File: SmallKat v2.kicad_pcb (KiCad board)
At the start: 4 copper layers, 104 x 56 mm, 272 parts, among them IC1 TPS562201DDCR, IC2 TPS40192DRCT, IC4 MAX34409ETE+, IC5 MAX34409ETE+, IC6 MAX34409ETE+, IC7 MAX34409ETE+, J1 Conn_01x03_Male, J10 Conn_01x03_Male, J11 Conn_01x03_Male, J12 Conn_01x03_Male, J13 Conn_01x03_Male, J14 Conn_01x03_Male, J15 Conn_01x03_Male, J16 Conn_01x03_Male, J17 Conn_01x03_Male, J19 USB_C_Receptacle, J2 Conn_01x03_Male, J21 Conn_01x05_Male, J3 Conn_01x03_Male, J4 Conn_01x03_Male, J5 Conn_01x03_Male, J6 Conn_01x03_Male, J7 Conn_01x03_Male, J8 Conn_01x03_Male, J9 Conn_01x02_Male, Q1 BUK9M120-100EX, Q10 CSD17307Q5A, Q11 CSD17307Q5A, Q12 Si7141DP, Q2 BUK9M120-100EX, Q3 MMBT3904, Q4 MMBT3904, Q7 2N3905, Q8 BUK9M120-100EX, Q9 BUK9M120-100EX, SW1 SW_SPST, SW2 SW_SPST, SW5 SW_SPST, U1 BNO055, U11 FUSB302BMPX, U12 BQ24770, U13 bq76925, U14 PCA9641, U2 LM2840Y, U3 ESP32-WROOM-32, U4 CP2102N-A01-GQFN24, U6 STM32L432KBUx, Y1 32.768kHz

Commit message: order
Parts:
- removed C22: 1uF, Capacitor_SMD:C_0402_1005Metric
- removed D17: MA2YD26, Diode_SMD:D_SOD-123F
- removed IC2: TPS40192DRCT, TPS40192DRCT:SON50P300X300X100-11N
- removed TP8: TestPoint, TestPoint:TestPoint_Pad_D1.5mm
- added C30: 22uF, Capacitor_SMD:C_0805_2012Metric, F.Cu at (186.5, 112.3)
- added C33: 0.1uF, Capacitor_SMD:C_0402_1005Metric, F.Cu at (190.5, 105.4)
- added C34: 22uF, Capacitor_SMD:C_0805_2012Metric, F.Cu at (186.5, 110.4)
- added D6: LED, LED_SMD:LED_0603_1608Metric, F.Cu at (142.7, 139.4)
- added IC3: TPS562201DDCR, Package_TO_SOT_SMD:SOT-23-6, F.Cu at (187.7, 104.0)
- added R28: 10K, Resistor_SMD:R_0402_1005Metric, F.Cu at (187.7, 101.1)
- added R29: 2.74K, Resistor_SMD:R_0402_1005Metric, F.Cu at (144.6, 104.0)
- added R30: 29.4R, Resistor_SMD:R_0402_1005Metric, F.Cu at (128.4, 96.9)
- added R31: 330R, Resistor_SMD:R_0402_1005Metric, F.Cu at (143.1, 138.1)
- added TP4: TestPoint, TestPoint:TestPoint_Pad_D1.5mm, B.Cu at (156.7, 88.4)
- C10: value 1000pF -> 10uF; footprint Capacitor_SMD:C_0402_1005Metric -> Capacitor_SMD:C_1206_3216Metric
- C11: value 100pF -> 10uF; footprint Capacitor_SMD:C_0402_1005Metric -> Capacitor_SMD:C_1206_3216Metric
- C12: value 10nF -> 2.2uF
- C13: value 1uF -> 0.1uF
- C14: value 4.7uF -> 6.8nF
- C15: value 470nF -> 0.1uF
- C16: value 10uF -> 5.6nF; footprint Capacitor_SMD:C_1206_3216Metric -> Capacitor_SMD:C_0402_1005Metric
- C18: value 10uF -> 1pF; footprint Capacitor_SMD:C_1206_3216Metric -> Capacitor_SMD:C_0402_1005Metric
- C19: value 100uF -> 330pF; footprint Capacitor_SMD:C_1210_3225Metric -> Capacitor_SMD:C_0402_1005Metric
- C21: value 100uF -> 10uF; footprint Capacitor_SMD:C_1210_3225Metric -> Capacitor_SMD:C_0805_2012Metric
- C23: value 2.2uF -> 10uF
- C25: value 0.1uF -> 10uF; footprint Capacitor_SMD:C_0402_1005Metric -> Capacitor_SMD:C_0805_2012Metric
- C35: value 10uF -> 0.1uF; footprint Capacitor_SMD:C_0805_2012Metric -> Capacitor_SMD:C_0402_1005Metric
- IC1: footprint TPS562201DDCR:SOT95P280X110-6N -> Package_TO_SOT_SMD:SOT-23-6
- J21: moved to B.Cu
- L3: value 15uH -> 4.7uH; footprint Inductor_SMD:L_1210_3225Metric -> Inductor_SMD:L_0805_2012Metric
- L4: value L -> 2.2uH
- R12: value 2.18k -> 20K
- R13: value 20k -> 2.1R
- R14: value 2.61k -> 10K
- R15: value 4.22k -> 10K
- R16: value 3.9k -> 20K
- R17: value 100k -> 20K
- R18: value 100k -> 634R
- R19: value 100k -> 2.49K
- R2: value 1K -> 10K
- R20: value 20K -> 18K
- R3: value 3.4K -> 33.2K
- U2: value LM2840Y -> LM25145RGYR; footprint Package_TO_SOT_SMD:TSOT-23-6 -> LM25145:LM25145RGYR
- moved U2 39.0 mm to (149.3, 103.3), turned to 0 degrees
- moved C10 22.6 mm to (160.2, 95.0)
- moved C18 19.4 mm to (142.7, 103.0), turned to 270 degrees
- moved TP7 19.3 mm to (130.8, 102.4)
- moved R20 16.9 mm to (143.7, 104.0), turned to 90 degrees
- moved C11 16.8 mm to (160.2, 97.3), turned to 0 degrees
- moved C16 15.2 mm to (146.0, 102.6)
- moved R12 14.7 mm to (127.2, 98.2)
- moved R13 13.8 mm to (152.2, 100.0), turned to 180 degrees
- moved TP6 11.5 mm to (145.2, 88.3)
- moved C19 8.85 mm to (128.3, 98.9), turned to 270 degrees
- moved C12 8.75 mm to (152.7, 104.1), turned to 0 degrees
- moved R14 8.18 mm to (148.1, 100.0), turned to 180 degrees
- moved R19 7.81 mm to (144.1, 102.6), turned to 0 degrees
- moved C13 7.71 mm to (150.3, 100.0), turned to 180 degrees
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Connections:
- C10 pad 1: +6V -> +BATT
- C10 pad 2: Net-(C10-Pad2) -> GND
- C11 pad 1: Net-(C11-Pad1) -> +BATT
- C11 pad 2: Net-(C11-Pad2) -> GND
- C12 pad 1: Net-(C11-Pad1) -> Net-(C12-Pad1)
- C12 pad 2: Net-(C12-Pad2) -> GND
- C13 pad 1: +BATT -> Net-(C13-Pad1)
- C16 pad 1: +BATT -> Net-(C16-Pad1)
- C16 pad 2: GND -> Net-(C16-Pad2)
- C18 pad 1: +BATT -> Net-(C18-Pad1)
- C18 pad 2: GND -> Net-(C16-Pad2)
- C19 pad 1: +6V -> Net-(C19-Pad1)
- C23 pad 1: VBUS -> GND
- C23 pad 2: GND -> +BATT
- C25 pad 1: Net-(C25-Pad1) -> GND
- C25 pad 2: Net-(C25-Pad2) -> +BATT
- C35 pad 1: +3.3VA -> Net-(C35-Pad1)
- C35 pad 2: GND -> Net-(C35-Pad2)
- L3 pad 1: Net-(C25-Pad1) -> +3.3VA
- L3 pad 2: +3.3VA -> Net-(C35-Pad2)
- Q1 pad 4: Net-(IC2-Pad10) -> Net-(Q1-Pad4)
- Q2 pad 4: Net-(IC2-Pad7) -> Net-(Q2-Pad4)
- R12 pad 1: Net-(C11-Pad2) -> +6V
- R12 pad 2: GND -> Net-(D4-Pad2)
- R13 pad 1: +6V -> +BATT
- R13 pad 2: Net-(C11-Pad2) -> Net-(C13-Pad1)
- R14 pad 1: Net-(C11-Pad2) -> Net-(R14-Pad1)
- R14 pad 2: Net-(C10-Pad2) -> /MainBoard/6VEN
- R15 pad 1: Net-(C12-Pad2) -> Net-(R15-Pad1)
- R15 pad 2: Net-(C11-Pad2) -> GND
- R16 pad 1: Net-(C11-Pad1) -> Net-(R16-Pad1)
- R16 pad 2: GND -> Net-(C12-Pad1)
- R17 pad 1: /MainBoard/6VEN -> Net-(R17-Pad1)
- R17 pad 2: Net-(IC2-Pad1) -> Net-(C12-Pad1)
- R18 pad 1: Net-(C14-Pad1) -> Net-(C15-Pad1)
- R18 pad 2: Net-(IC2-Pad5) -> Net-(R18-Pad2)
- R19 pad 1: Net-(C15-Pad1) -> Net-(C18-Pad1)
- R19 pad 2: Net-(C15-Pad2) -> Net-(C16-Pad1)
- R2 pad 1: Net-(R2-Pad1) -> GND
- R2 pad 2: GND -> Net-(IC3-Pad4)
- R20 pad 2: Net-(D4-Pad2) -> Net-(C18-Pad1)
- R3 pad 2: Net-(R2-Pad1) -> Net-(IC3-Pad4)
- TP6 pad 1: +BATT -> GND
- TP7 pad 1: GND -> +6V
- U2 pad 1: Net-(C25-Pad2) -> Net-(R14-Pad1)
- U2 pad 2: GND -> Net-(R15-Pad1)
- U2 pad 3: Net-(R2-Pad1) -> Net-(C14-Pad1)
- U2 pad 4: VBUS -> Net-(C16-Pad2)
- U2 pad 5: VBUS -> Net-(C18-Pad1)
- U2 pad 6: Net-(C25-Pad1) -> GND
- U3 pad 39: (no net) -> GND
- U6 pad 18: (no net) -> Net-(R31-Pad2)
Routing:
- net +BATT: track 51.0 -> 79.8 mm, vias 10 -> 19
- net GND: track 116.1 -> 131.7 mm, vias 576 -> 532
- net VBUS: track 11.4 -> 0.00 mm, vias 416 -> 214
- net Net-(Q2-Pad4): track 0.00 -> 10.5 mm, vias 0 -> 2
- net Net-(C12-Pad1): track 0.00 -> 9.96 mm, vias 0 -> 2
- net Net-(R31-Pad2): track 0.00 -> 9.50 mm, vias 0 -> 2
- net Net-(C11-Pad2): track 7.95 -> 0.00 mm
- net Net-(IC2-Pad7): track 6.45 -> 0.00 mm, vias 3 -> 0
- net Net-(C16-Pad2): track 0.00 -> 6.34 mm, vias 0 -> 2
- net Net-(C18-Pad1): track 0.00 -> 6.24 mm
- net Net-(C25-Pad1): track 6.10 -> 0.00 mm
- net Net-(C11-Pad1): track 5.63 -> 0.00 mm, vias 2 -> 0
- net Net-(Q1-Pad4): track 0.00 -> 5.46 mm, vias 0 -> 2
- net Net-(C35-Pad2): track 0.00 -> 5.41 mm, vias 0 -> 2
- net Net-(IC2-Pad10): track 4.78 -> 0.00 mm, vias 1 -> 0
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
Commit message: Rev
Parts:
- removed C45, C46, C54, C55: 0.1uF, Capacitor_SMD:C_0402_1005Metric
- removed C82: 1uF, Capacitor_SMD:C_0402_1005Metric
- removed IC4, IC5, IC6, IC7: MAX34409ETE+, MAX34409ETE+:QFN65P400X400X80-17N
- removed Q4: MMBT3904, Package_TO_SOT_SMD:SOT-23
- removed R101, R102, R103, R106, R107, R108, R109, R111, R112, R113, R114, R59, R60, R64, R65, R67, R68, R71, R72, R76, R77, R81, R82, R84, R85, R89, R90, R93, R94, R95, R96, R98: 100R, Resistor_SMD:R_0402_1005Metric
- removed R110, R83, R97: 0R, Resistor_SMD:R_0402_1005Metric
- removed R126, R127, R43: 10K, Resistor_SMD:R_0402_1005Metric
- removed U14: PCA9641, Package_DFN_QFN:UQFN-16-1EP_4x4mm_P0.65mm_EP2.6x2.6mm
- removed U2: LM25145RGYR, LM25145:LM25145RGYR
- removed U6: STM32L432KBUx, Package_DFN_QFN:QFN-32-1EP_5x5mm_P0.5mm_EP3.45x3.45mm
- added C22: C, Capacitor_SMD:C_0402_1005Metric, F.Cu at (129.2, 114.6)
- added C36: C, Capacitor_SMD:C_0402_1005Metric, F.Cu at (129.3, 116.5)
- added C38: C, Capacitor_SMD:C_0402_1005Metric, F.Cu at (125.0, 119.9)
- added C39: 47uF, Capacitor_SMD:C_1206_3216Metric, F.Cu at (127.2, 92.6)
- added C40: 47uF, Capacitor_SMD:C_1206_3216Metric, F.Cu at (127.2, 90.4)
- added C41: 1uF, Capacitor_SMD:C_0402_1005Metric, F.Cu at (91.5, 85.2)
- added C42: 0.1uF, Capacitor_SMD:C_0402_1005Metric, F.Cu at (148.0, 123.5)
- added C43: 0.1uF, Capacitor_SMD:C_0402_1005Metric, F.Cu at (157.6, 94.8)
- added D9: LED, LED_SMD:LED_0603_1608Metric, F.Cu at (146.8, 108.7)
- added F5: Fuse, 01550900M:0154.250DR, F.Cu at (151.1, 113.2)
- added IC8: TPS40192DRCT-TPS40192DRCT, Package_SON:VSON-10-1EP_3x3mm_P0.5mm_EP1.2x2mm, F.Cu at (120.2, 95.5)
- added J18: Conn_01x03_Male, Connector_PinHeader_2.54mm:PinHeader_1x03_P2.54mm_Vertical, F.Cu at (160.0, 110.7)
- added J20: Conn_01x03_Male, Connector_PinHeader_2.54mm:PinHeader_1x03_P2.54mm_Vertical, F.Cu at (160.0, 105.7)
- added J22: Conn_01x03_Male, Connector_PinHeader_2.54mm:PinHeader_1x03_P2.54mm_Vertical, F.Cu at (160.0, 108.2)
- added J23: Conn_01x03_Male, Connector_PinHeader_2.54mm:PinHeader_1x03_P2.54mm_Vertical, F.Cu at (160.0, 103.1)
- added PS1: PAC1934T-I_JQ, PAC1934T-I_JQ:QFN65P400X400X55-17N-D, F.Cu at (83.7, 93.5)
- added PS2: PAC1934T-I_JQ, PAC1934T-I_JQ:QFN65P400X400X55-17N-D, F.Cu at (84.9, 113.6)
- added PS3: PAC1934T-I_JQ, PAC1934T-I_JQ:QFN65P400X400X55-17N-D, F.Cu at (84.1, 127.3)
- added PS4: PAC1934T-I_JQ, PAC1934T-I_JQ:QFN65P400X400X55-17N-D, F.Cu at (149.0, 126.7)
- added PS5: PAC1934T-I_JQ, PAC1934T-I_JQ:QFN65P400X400X55-17N-D, F.Cu at (158.3, 98.0)
- added R128: 20K, Resistor_SMD:R_0402_1005Metric, F.Cu at (147.6, 110.4)
- added R32: 3.3K, Resistor_SMD:R_0402_1005Metric, F.Cu at (126.9, 119.9)
- added R33: 0.01R, Resistor_SMD:R_0603_1608Metric, F.Cu at (156.7, 112.5)
- added R34: 0.01R, Resistor_SMD:R_0603_1608Metric, F.Cu at (156.7, 106.9)
- added R35: 0.01R, Resistor_SMD:R_0603_1608Metric, F.Cu at (156.7, 109.4)
- added R36: 0.01R, Resistor_SMD:R_0603_1608Metric, F.Cu at (156.7, 104.5)
- added R39: 0R, Resistor_SMD:R_0402_1005Metric, F.Cu at (148.2, 129.7)
- added R40: 0R, Resistor_SMD:R_0402_1005Metric, F.Cu at (157.2, 101.1)
- added TP8: TestPoint, TestPoint:TestPoint_Pad_D1.5mm, B.Cu at (120.8, 118.0)
- added U5: LPC824M201JHI33, Package_DFN_QFN:QFN-32-1EP_5x5mm_P0.5mm_EP3.45x3.45mm, F.Cu at (125.6, 115.6)
- added U7: TLC5947RHB, Package_DFN_QFN:QFN-32-1EP_5x5mm_P0.5mm_EP3.45x3.45mm, F.Cu at (125.3, 123.6)
- C10: value 10uF -> 1000pF; footprint Capacitor_SMD:C_1206_3216Metric -> Capacitor_SMD:C_0402_1005Metric
- C11: value 10uF -> 100pF; footprint Capacitor_SMD:C_1206_3216Metric -> Capacitor_SMD:C_0402_1005Metric
- C12: value 2.2uF -> 10nF
- C13: value 0.1uF -> 1uF
- C14: value 6.8nF -> 4.7uF
- C15: value 0.1uF -> 470nF
- C16: value 5.6nF -> 10uF; footprint Capacitor_SMD:C_0402_1005Metric -> Capacitor_SMD:C_1206_3216Metric
- C18: value 1pF -> 10uF; footprint Capacitor_SMD:C_0402_1005Metric -> Capacitor_SMD:C_1206_3216Metric
- C19: value 330pF -> 100uF; footprint Capacitor_SMD:C_0402_1005Metric -> Capacitor_SMD:C_1210_3225Metric
- C21: value 10uF -> 100uF; footprint Capacitor_SMD:C_0805_2012Metric -> Capacitor_SMD:C_1210_3225Metric
- C69, C74: footprint Capacitor_SMD:C_0402_1005Metric -> Capacitor_SMD:C_0805_2012Metric
- H1, H2, H3, H4: footprint MountingHole:MountingHole_2.7mm_M2.5_Pad_Via -> MountingHole:MountingHole_3.2mm_M3_Pad_Via
- J19: footprint Connector_USB:USB_C_Receptacle_Amphenol_12401610E4-2A_CircularHoles -> C167321:C167321
- J9: footprint SmallKat ESP32:SHDR2W320P716_1X2_1574X813X1588P -> XT30PB:XT30PB
- Q3: value MMBT3904 -> MBT3904DW1; footprint Package_TO_SOT_SMD:SOT-23 -> Package_TO_SOT_SMD:SOT-363_SC-70-6
- R12: value 20K -> 2.18k
- R123: footprint Resistor_SMD:R_0603_1608Metric -> Resistor_SMD:R_0805_2012Metric
- R13: value 2.1R -> 20k
- R14: value 10K -> 2.61k
- R15: value 10K -> 4.22k
- R16: value 20K -> 3.9k
- R17: value 20K -> 100k
- R18: value 634R -> 100k
- R19: value 2.49K -> 100k
- R20: value 18K -> 1K
- R29: value 2.74K -> 0R
- R30: value 29.4R -> 0R
- TP4, TP6, TP7: footprint TestPoint:TestPoint_Pad_D1.5mm -> TestPoint:TestPoint_Pad_D2.5mm
- moved J2 119.1 mm to (76.2, 119.9), turned to 270 degrees
- moved J8 118.8 mm to (76.2, 127.5), turned to 270 degrees
- moved J4 118.8 mm to (76.2, 122.4), turned to 270 degrees
- moved J6 118.7 mm to (76.2, 125.0), turned to 270 degrees
- moved R62 112.4 mm to (79.6, 121.1), turned to 0 degrees
- moved R80 112.0 mm to (79.5, 129.0), turned to 0 degrees
- moved R70 111.9 mm to (79.6, 123.7), turned to 0 degrees
- moved R75 111.8 mm to (79.5, 126.2), turned to 0 degrees
- moved H1 103.9 mm to (71.8, 85.4)
- moved F3 101.9 mm to (80.6, 134.4), turned to 180 degrees
- moved R78 100.5 mm to (87.7, 135.4), turned to 270 degrees
- moved D25 99.6 mm to (89.0, 135.1), turned to 270 degrees
- moved C52 88.1 mm to (85.0, 130.5)
- moved R2 73.8 mm to (116.7, 100.8), turned to 270 degrees
- moved R28 71.8 mm to (115.9, 102.9)
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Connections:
- C10 pad 1: +BATT -> +6V
- C10 pad 2: GND -> Net-(C10-Pad2)
- C11 pad 1: +BATT -> Net-(C11-Pad1)
- C11 pad 2: GND -> Net-(C11-Pad2)
- C12 pad 1: Net-(C12-Pad1) -> Net-(C11-Pad1)
- C12 pad 2: GND -> Net-(C12-Pad2)
- C13 pad 1: Net-(C13-Pad1) -> +BATT
- C16 pad 1: Net-(C16-Pad1) -> +BATT
- C16 pad 2: Net-(C16-Pad2) -> GND
- C18 pad 1: Net-(C18-Pad1) -> +BATT
- C18 pad 2: Net-(C16-Pad2) -> GND
- C19 pad 1: Net-(C19-Pad1) -> +6V
- C37 pad 1: +3.3VA -> +3V3
- Q3 pad 1: Net-(Q3-Pad1) -> /MainBoard/ESP32Module/RTS
- Q3 pad 2: /MainBoard/ESP32Module/RTS -> Net-(Q3-Pad2)
- Q3 pad 3: /MainBoard/ESP32Module/EN -> /MainBoard/ESP32Module/DTR
- R12 pad 1: +6V -> Net-(C11-Pad2)
- R12 pad 2: Net-(D4-Pad2) -> GND
- R13 pad 1: +BATT -> +6V
- R13 pad 2: Net-(C13-Pad1) -> Net-(C11-Pad2)
- R14 pad 1: Net-(R14-Pad1) -> Net-(C11-Pad2)
- R14 pad 2: /MainBoard/6VEN -> Net-(C10-Pad2)
- R15 pad 1: Net-(R15-Pad1) -> Net-(C12-Pad2)
- R15 pad 2: GND -> Net-(C11-Pad2)
- R16 pad 1: Net-(R16-Pad1) -> Net-(C11-Pad1)
- R16 pad 2: Net-(C12-Pad1) -> GND
- R17 pad 1: Net-(R17-Pad1) -> /MainBoard/6VEN
- R17 pad 2: Net-(C12-Pad1) -> Net-(IC8-Pad1)
- R18 pad 1: Net-(C15-Pad1) -> Net-(C14-Pad1)
- R19 pad 1: Net-(C18-Pad1) -> Net-(C15-Pad1)
- R19 pad 2: Net-(C16-Pad1) -> Net-(C15-Pad2)
- R20 pad 2: Net-(C18-Pad1) -> Net-(D4-Pad2)
- R21 pad 1: /MainBoard/SERVO0 -> /MainBoard/NRST
- R25 pad 1: Net-(Q3-Pad1) -> Net-(Q3-Pad2)
- R26 pad 1: Net-(Q4-Pad1) -> Net-(Q3-Pad5)
- R29 pad 1: Net-(C18-Pad1) -> Net-(PS2-Pad6)
- R29 pad 2: GND -> +3V3
- R30 pad 1: +6V -> Net-(PS3-Pad6)
- R30 pad 2: Net-(C19-Pad1) -> +3V3
- R66 pad 1: +3V3 -> Net-(PS1-Pad6)
- R66 pad 2: Net-(IC4-Pad14) -> +3V3
- TP4 pad 1: +BATT -> +6V
- TP6 pad 1: GND -> +BATT
- TP7 pad 1: +6V -> GND
- U3 pad 10: /MainBoard/SERVO4 -> (no net)
- U3 pad 11: /MainBoard/SERVO3 -> (no net)
- U3 pad 12: /MainBoard/SERVO2 -> /MainBoard/TX1
- U3 pad 13: /MainBoard/SERVO1 -> /MainBoard/RX1
- U3 pad 14: /MainBoard/SERVO0 -> /MainBoard/NRST
- U3 pad 16: /MainBoard/SERVO8 -> /MainBoard/TALKALLOWED
- U3 pad 23: /MainBoard/SERVO9 -> (no net)
- U3 pad 24: /MainBoard/SERVO10 -> (no net)
- U3 pad 26: /MainBoard/SERVO11 -> (no net)
- U3 pad 27: /MainBoard/SERVO12 -> (no net)
- U3 pad 28: /MainBoard/SERVO13 -> (no net)
- U3 pad 29: /MainBoard/SERVO14 -> (no net)
- U3 pad 30: /MainBoard/SERVO15 -> (no net)
- U3 pad 31: /MainBoard/SERVO7 -> (no net)
- U3 pad 8: /MainBoard/SERVO6 -> (no net)
- U3 pad 9: /MainBoard/SERVO5 -> (no net)
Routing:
- net /MainBoard/_SCL: track 131.4 -> 0.00 mm, vias 6 -> 0
- net /MainBoard/_SDA: track 128.6 -> 0.00 mm, vias 7 -> 0
- net /MainBoard/SCL: track 38.7 -> 154.9 mm, vias 5 -> 14
- net /MainBoard/SDA: track 39.6 -> 155.3 mm, vias 5 -> 13
- net /MainBoard/Servos/6V4: track 111.9 -> 3.60 mm, vias 104 -> 0
- net /MainBoard/Servos/6V1: track 104.9 -> 0.00 mm, vias 164 -> 0
- net /MainBoard/Servos/6V3: track 90.1 -> 4.12 mm, vias 71 -> 0
- net /MainBoard/SERVO0: track 16.4 -> 98.7 mm, vias 1 -> 2
- net /MainBoard/Servos/6V2: track 66.7 -> 3.92 mm, vias 64 -> 0
- net Net-(R24-Pad2): track 7.54 -> 62.5 mm, vias 2 -> 5
- net /MainBoard/SERVO1: track 17.8 -> 61.6 mm, vias 1 -> 2
- net /MainBoard/SERVO19: track 0.00 -> 43.4 mm, vias 0 -> 1
- net +3.3VA: track 63.7 -> 21.7 mm, vias 19 -> 4
- net /MainBoard/SERVO18: track 0.00 -> 41.2 mm, vias 0 -> 1
- net /MainBoard/SERVO2: track 20.9 -> 60.8 mm, vias 1 -> 2
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- added copper zone on F.Cu, net /MainBoard/Servos/6V1
- added copper zone on F.Cu, net /MainBoard/Servos/6V2
- added copper zone on F.Cu, net /MainBoard/Servos/6V3
- added copper zone on F.Cu, net /MainBoard/Servos/6V4
- added copper zone on F.Cu, net /MainBoard/Servos/6V5
- removed copper zone on In1.Cu, net +3.3VA
- removed copper zone on In1.Cu, net GND
- removed copper zone on F.Cu, net Net-(C50-Pad2)
- removed copper zone on F.Cu, net Net-(C57-Pad1)
- removed copper zone on In1.Cu, net VBUS
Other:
- board size 104 x 56 mm -> 100 x 56 mm
- net class Default: clearance 0.127 -> 0.1778; trace_width 0.127 -> 0.1778
- rule trace_clearance: 0.127 -> 0.1778
- board text removed: "+"
- board text removed: "BATT+"
- board text removed: "Elbow"
- board text removed: "Fuse Good"
- board text removed: "Head Pan"
- board text removed: "Head Tilt"
- board text removed: "Pan"
- board text removed: "Tail Pan"
- board text removed: "Tail Tilt"
- board text removed: "Tilt"

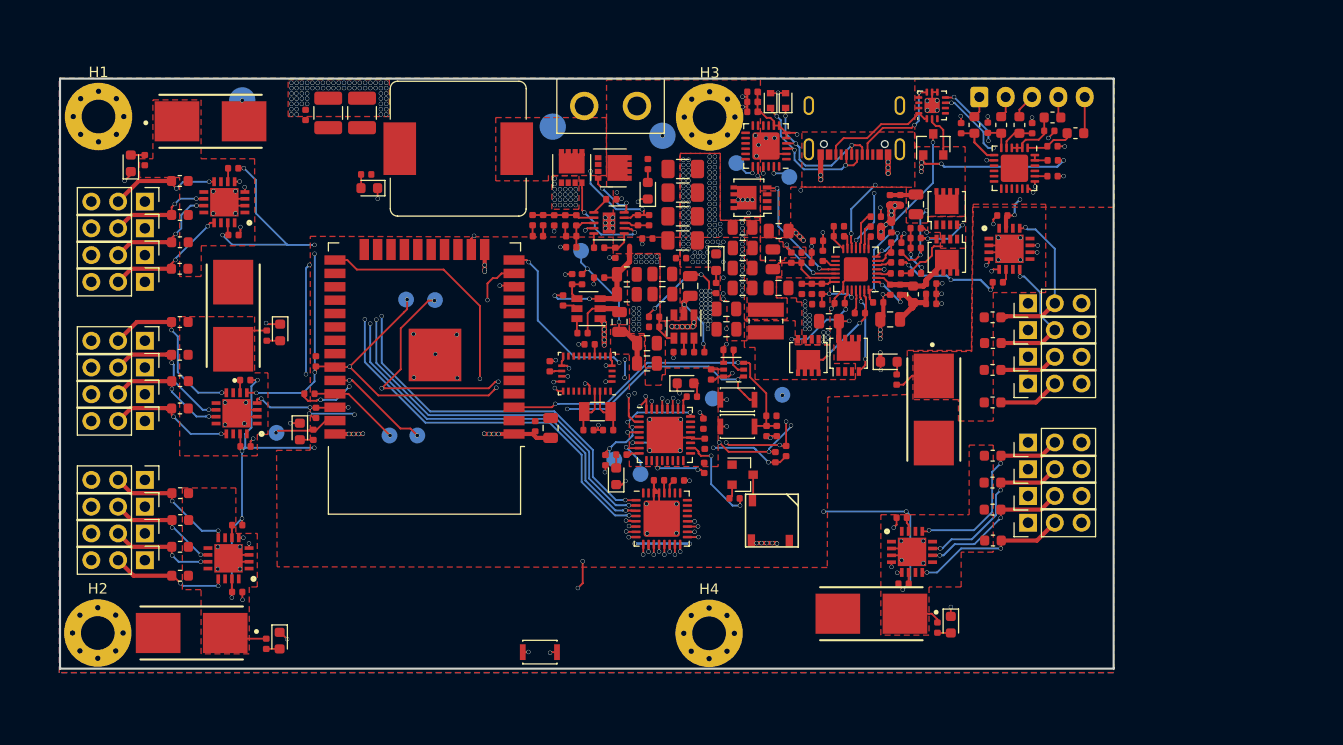
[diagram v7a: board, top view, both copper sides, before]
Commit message: This rev removes the safety micro and instead uses the dji battery
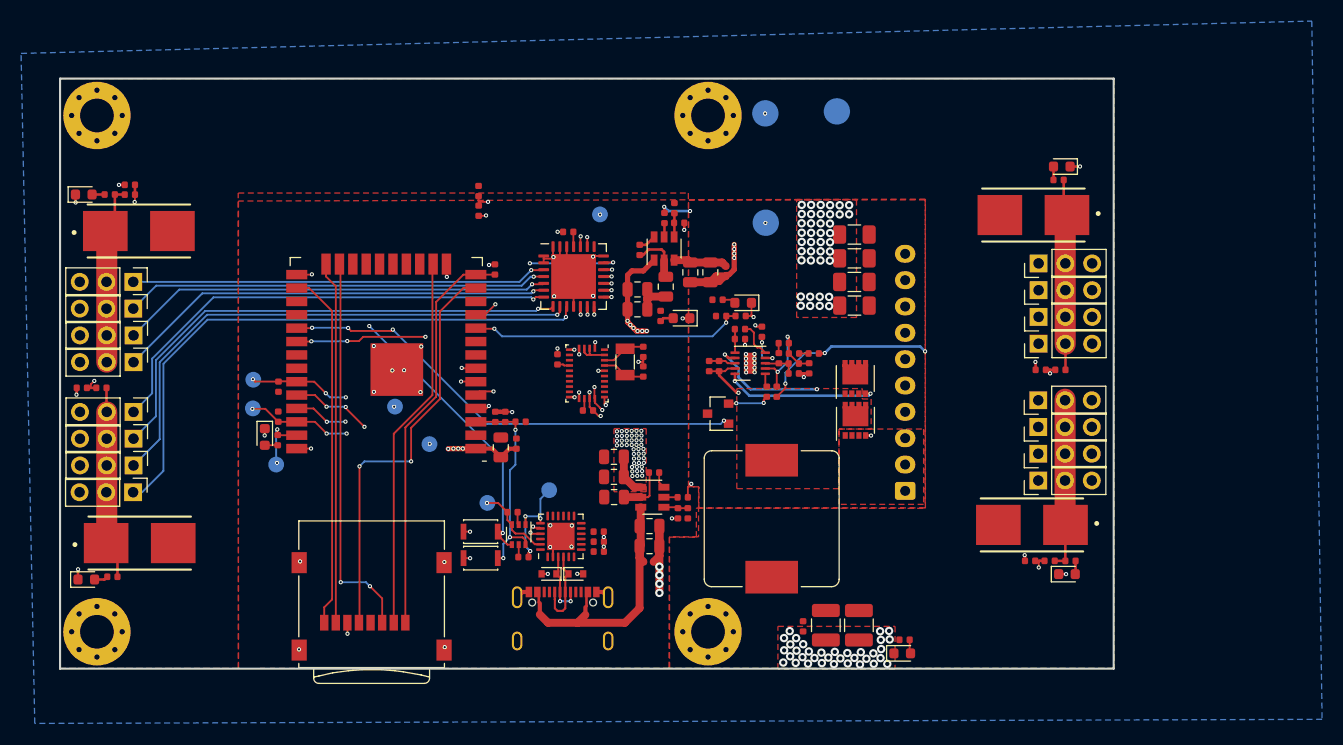
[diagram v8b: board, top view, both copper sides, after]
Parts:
- removed BZ1: Buzzer, KLJ-5030:KLJ-5030
- removed C34, C72, C75, C76, C77: 22uF, Capacitor_SMD:C_0805_2012Metric
- removed C35, C37, C42, C43, C49, C51, C52, C53, C57, C59, C64, C70, C71, C73, C78, C79, C80: 0.1uF, Capacitor_SMD:C_0402_1005Metric
- removed C36, C38: C, Capacitor_SMD:C_0402_1005Metric
- removed C47: 2.2uF, Capacitor_SMD:C_0805_2012Metric
- removed C48: 2200pF, Capacitor_SMD:C_0402_1005Metric
- removed C50, C60, C61, C65, C81: 1uF, Capacitor_SMD:C_0402_1005Metric
- removed C56, C58: 100pF, Capacitor_SMD:C_0402_1005Metric
- removed C62: 0.01uF, Capacitor_SMD:C_0402_1005Metric
- removed C63, C66, C69, C74: 10uF, Capacitor_SMD:C_0805_2012Metric
- removed C67: 470pF, Capacitor_SMD:C_0402_1005Metric
- removed C68: 0.047uF, Capacitor_SMD:C_0402_1005Metric
- removed D18, D6, D9: LED, LED_SMD:LED_0603_1608Metric
- removed D5: BAT54C, Package_TO_SOT_SMD:SOT-23
- removed F5: Fuse, 01550900M:0154.250DR
- removed IC3: TPS562201DDCR, Package_TO_SOT_SMD:SOT-23-6
- removed J20, J22, J23: Conn_01x03_Male, Connector_PinHeader_2.54mm:PinHeader_1x03_P2.54mm_Vertical
- removed J21: Conn_01x05_Male, Connector_JST:JST_EH_S5B-EH_1x05_P2.50mm_Horizontal
- removed L4: 2.2uH, Inductor_SMD:L_Wuerth_MAPI-3020
- removed PS1, PS2, PS3, PS4, PS5: PAC1934T-I_JQ, PAC1934T-I_JQ:QFN65P400X400X55-17N-D
- removed Q10, Q11: CSD17307Q5A, Package_TO_SOT_SMD:LFPAK33
- removed Q12: Si7141DP, Package_TO_SOT_SMD:LFPAK33
- removed Q7: 2N3905, Package_TO_SOT_SMD:SOT-23
- removed Q8, Q9: BUK9M120-100EX, Package_TO_SOT_SMD:LFPAK33
- removed R100, R104, R105, R57, R61, R62, R69, R70, R74, R75, R79, R80, R87, R88, R91, R92, R99: 0.01R, Resistor_SMD:R_0603_1608Metric
- removed R117, R119, R125, R45, R46, R47, R48, R56: 10K, Resistor_SMD:R_0402_1005Metric
- removed R118: 3M, Resistor_SMD:R_0402_1005Metric
- removed R120: 316K, Resistor_SMD:R_0402_1005Metric
- removed R121: 100K, Resistor_SMD:R_0402_1005Metric
- removed R122: 10R, Resistor_SMD:R_0402_1005Metric
- removed R123: 0.01R, Resistor_SMD:R_0805_2012Metric
- removed R124: 47R, Resistor_SMD:R_0603_1608Metric
- removed R128: 20K, Resistor_SMD:R_0402_1005Metric
- removed R24: 470R, Resistor_SMD:R_0402_1005Metric
- removed R39, R40, R66: 0R, Resistor_SMD:R_0402_1005Metric
- removed R44: 330R, Resistor_SMD:R_0402_1005Metric
- removed R49, R52: 3.9K, Resistor_SMD:R_0402_1005Metric
- removed R50: 430K, Resistor_SMD:R_0402_1005Metric
- removed R51: 66.5K, Resistor_SMD:R_0402_1005Metric
- removed R53: 4.7R, Resistor_SMD:R_0402_1005Metric
- removed R54, R55: 4.02K, Resistor_SMD:R_0402_1005Metric
- removed R58: 30.1K, Resistor_SMD:R_0402_1005Metric
- removed SW5: SW_SPST, Button_Switch_SMD:SW_SPST_CK_KXT3
- removed TP20, TP21, TP22, TP23, TP8: TestPoint, TestPoint:TestPoint_Pad_D1.5mm
- removed U11: FUSB302BMPX, Package_DFN_QFN:WQFN-14-1EP_2.5x2.5mm_P0.5mm_EP1.45x1.45mm
- removed U12: BQ24770, Package_DFN_QFN:QFN-28-1EP_4x4mm_P0.4mm_EP2.3x2.3mm
- removed U13: bq76925, Package_DFN_QFN:QFN-24-1EP_4x4mm_P0.5mm_EP2.6x2.6mm
- removed U5: LPC824M201JHI33, Package_DFN_QFN:QFN-32-1EP_5x5mm_P0.5mm_EP3.45x3.45mm
- removed U7: TLC5947RHB, Package_DFN_QFN:QFN-32-1EP_5x5mm_P0.5mm_EP3.45x3.45mm
- added IC2: TPS562201DDCR, Package_TO_SOT_SMD:SOT-23-6, F.Cu at (124.4, 121.5)
- added Q5: DMG2301L, Package_TO_SOT_SMD:SOT-23, F.Cu at (130.6, 113.6)
- added U2: PCA9685BS, Package_DFN_QFN:QFN-28-1EP_6x6mm_P0.65mm_EP4.25x4.25mm, F.Cu at (116.9, 100.6)
- C20: value 0.1uF -> 10uF; footprint Capacitor_SMD:C_0402_1005Metric -> Capacitor_SMD:C_0805_2012Metric
- C22: value C -> 10uF; footprint Capacitor_SMD:C_0402_1005Metric -> Capacitor_SMD:C_0805_2012Metric
- C23: value 10uF -> 22uF
- C25: value 10uF -> 0.1uF; footprint Capacitor_SMD:C_0805_2012Metric -> Capacitor_SMD:C_0402_1005Metric
- J18: value Conn_01x03_Male -> Micro_SD_Card; footprint Connector_PinHeader_2.54mm:PinHeader_1x03_P2.54mm_Vertical -> Connector_Card:microSD_HC_Wuerth_693072010801
- J9: value Conn_01x02_Male -> Conn_01x10_Female; footprint XT30PB:XT30PB -> Connector_JST:JST_EH_B10B-EH-A_1x10_P2.50mm_Vertical; moved to B.Cu
- R22, R37: value 47R -> 10K; footprint Resistor_SMD:R_0603_1608Metric -> Resistor_SMD:R_0402_1005Metric
- R23, R38: value 47R -> 8.2K; footprint Resistor_SMD:R_0603_1608Metric -> Resistor_SMD:R_0402_1005Metric
- R29: value 0R -> 33.2K
- R3: value 33.2K -> 2.4K
- R30: value 0R -> 10K
- R31: value 330R -> 10K
- R32: value 3.3K -> 8.2K
- R33, R35: value 0.01R -> 10K; footprint Resistor_SMD:R_0603_1608Metric -> Resistor_SMD:R_0402_1005Metric
- R34, R36: value 0.01R -> 8.2K; footprint Resistor_SMD:R_0603_1608Metric -> Resistor_SMD:R_0402_1005Metric
- moved R34 86.6 mm to (70.2, 111.2)
- moved J8 86.1 mm to (161.0, 112.3), turned to 90 degrees
- moved J6 85.4 mm to (161.0, 114.9), turned to 90 degrees
- moved J4 84.9 mm to (161.0, 117.4), turned to 90 degrees
- moved J2 84.8 mm to (161.0, 119.9), turned to 90 degrees
- moved R33 84.6 mm to (72.1, 111.2)
- moved F3 80.4 mm to (160.4, 124.2)
- moved R78 76.7 mm to (164.0, 127.6), turned to 0 degrees
- moved H4 76.1 mm to (71.7, 85.3)
- moved D25 75.0 mm to (163.7, 128.8), turned to 0 degrees
- moved C21 67.8 mm to (140.8, 133.7), turned to 270 degrees
- moved C19 67.7 mm to (144.0, 133.7), turned to 270 degrees
- moved C41 67.7 mm to (138.7, 133.8), turned to 270 degrees
- moved R20 67.5 mm to (148.3, 135.1), turned to 0 degrees
- moved D4 67.1 mm to (148.1, 136.3), turned to 0 degrees
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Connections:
- C17 pad 1: Net-(C17-Pad1) -> +3V3
- C20 pad 1: Net-(C20-Pad1) -> GND
- C20 pad 2: GND -> VBUS
- C22 pad 2: +3.3VA -> VBUS
- C23 pad 1: GND -> +3V3
- C23 pad 2: +BATT -> GND
- C25 pad 2: +BATT -> VBUS
- C30 pad 1: +3.3VA -> +3V3
- C33 pad 1: GND -> Net-(C33-Pad1)
- C33 pad 2: +BATT -> Net-(C33-Pad2)
- H3 pad 1: +BATT -> +6V
- J1 pad 2: /MainBoard/Servos/S1 -> /MainBoard/Servos/6V1
- J10 pad 2: /MainBoard/Servos/S5 -> /MainBoard/Servos/6V2
- J11 pad 2: /MainBoard/Servos/S13 -> /MainBoard/Servos/6V4
- J12 pad 2: /MainBoard/Servos/S6 -> /MainBoard/Servos/6V2
- J13 pad 2: /MainBoard/Servos/S14 -> /MainBoard/Servos/6V4
- J14 pad 2: /MainBoard/Servos/S7 -> /MainBoard/Servos/6V2
- J15 pad 2: /MainBoard/Servos/S15 -> /MainBoard/Servos/6V4
- J16 pad 2: /MainBoard/Servos/S8 -> /MainBoard/Servos/6V2
- J17 pad 2: /MainBoard/Servos/S16 -> /MainBoard/Servos/6V4
- J18 pad 1: /MainBoard/SERVO16 -> /MainBoard/IO12
- J18 pad 2: /MainBoard/Servos/S17 -> /MainBoard/IO13
- J18 pad 3: GND -> /MainBoard/IO15
- J19 pad A5: /MainBoard/CC1 -> (no net)
- J19 pad B5: /MainBoard/CC2 -> (no net)
- J2 pad 2: /MainBoard/Servos/S9 -> /MainBoard/Servos/6V3
- J3 pad 2: /MainBoard/Servos/S2 -> /MainBoard/Servos/6V1
- J4 pad 2: /MainBoard/Servos/S10 -> /MainBoard/Servos/6V3
- J5 pad 2: /MainBoard/Servos/S3 -> /MainBoard/Servos/6V1
- J6 pad 2: /MainBoard/Servos/S11 -> /MainBoard/Servos/6V3
- J7 pad 2: /MainBoard/Servos/S4 -> /MainBoard/Servos/6V1
- J8 pad 2: /MainBoard/Servos/S12 -> /MainBoard/Servos/6V3
- J9 pad 2: +BATT -> GND
- L3 pad 1: +3.3VA -> +3V3
- L3 pad 2: Net-(C35-Pad2) -> Net-(C33-Pad2)
- R10 pad 1: /MainBoard/3.3VEN -> +BATT
- R17 pad 1: /MainBoard/6VEN -> Net-(Q5-Pad2)
- R2 pad 1: GND -> +BATT
- R2 pad 2: Net-(IC3-Pad4) -> /MainBoard/BATT_VOLTAGE
- R21 pad 1: /MainBoard/NRST -> /MainBoard/IO12
- R22 pad 1: Net-(C17-Pad1) -> +6V
- R22 pad 2: /MainBoard/BatteryBalancer/C4 -> /MainBoard/MEASURED_6V
- R23 pad 1: Net-(C20-Pad1) -> /MainBoard/MEASURED_6V
- R23 pad 2: /MainBoard/BatteryBalancer/C3 -> GND
- R28 pad 1: +BATT -> GND
- R28 pad 2: Net-(IC3-Pad5) -> Net-(IC2-Pad4)
- R29 pad 1: Net-(PS2-Pad6) -> +3V3
- R29 pad 2: +3V3 -> Net-(IC2-Pad4)
- R3 pad 1: +3.3VA -> /MainBoard/BATT_VOLTAGE
- R3 pad 2: Net-(IC3-Pad4) -> GND
- R30 pad 1: Net-(PS3-Pad6) -> +BATT
- R30 pad 2: +3V3 -> Net-(IC2-Pad5)
- R31 pad 1: Net-(D6-Pad2) -> /MainBoard/Servos/6V1
- R31 pad 2: Net-(R31-Pad2) -> MEASURED_FUSE1
- R32 pad 1: Net-(R32-Pad1) -> MEASURED_FUSE1
- R33 pad 1: /MainBoard/Servos/S17 -> /MainBoard/Servos/6V2
- R33 pad 2: /MainBoard/Servos/6V5 -> MEASURED_FUSE2
- R34 pad 1: /MainBoard/Servos/S19 -> MEASURED_FUSE2
- R34 pad 2: /MainBoard/Servos/6V5 -> GND
- R35 pad 1: /MainBoard/Servos/S18 -> /MainBoard/Servos/6V3
- R35 pad 2: /MainBoard/Servos/6V5 -> MEASURED_FUSE3
- R36 pad 1: /MainBoard/Servos/S20 -> MEASURED_FUSE3
- R36 pad 2: /MainBoard/Servos/6V5 -> GND
- R37 pad 1: Net-(C78-Pad1) -> /MainBoard/Servos/6V4
- R37 pad 2: /MainBoard/BatteryBalancer/C2 -> MEASURED_FUSE4
- R38 pad 1: Net-(C79-Pad1) -> MEASURED_FUSE4
- R38 pad 2: /MainBoard/BatteryBalancer/C1 -> GND
- U3 pad 10: (no net) -> /MainBoard/BATT_VOLTAGE
- U3 pad 11: (no net) -> /MainBoard/MEASURED_6V
- U3 pad 12: /MainBoard/TX1 -> (no net)
- U3 pad 13: /MainBoard/RX1 -> /MainBoard/IO14
- U3 pad 14: /MainBoard/NRST -> /MainBoard/IO12
- U3 pad 16: /MainBoard/TALKALLOWED -> /MainBoard/IO13
- U3 pad 23: (no net) -> /MainBoard/IO15
- U3 pad 24: (no net) -> /MainBoard/IO2
- U3 pad 26: (no net) -> /MainBoard/IO4
- U3 pad 29: (no net) -> /MainBoard/6VEN
- U3 pad 30: (no net) -> /MainBoard/EN_SERVO_DRIVER
- U3 pad 4: (no net) -> MEASURED_FUSE3
- U3 pad 5: (no net) -> MEASURED_FUSE4
- U3 pad 6: (no net) -> MEASURED_FUSE2
- U3 pad 7: (no net) -> MEASURED_FUSE1
- U4 pad 20: Net-(R24-Pad2) -> /MainBoard/ESP32Module/TXD
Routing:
- net +3V3: track 129.9 -> 8.25 mm, vias 51 -> 1
- net /MainBoard/SDA: track 155.3 -> 53.9 mm, vias 13 -> 5
- net /MainBoard/SCL: track 154.9 -> 54.5 mm, vias 14 -> 6
- net /MainBoard/SAFETYSCL: track 69.8 -> 0.00 mm, vias 9 -> 0
- net /MainBoard/SAFETYSDA: track 69.2 -> 0.00 mm, vias 9 -> 0
- net Net-(R24-Pad2): track 62.5 -> 0.00 mm, vias 5 -> 0
- net MEASURED_FUSE3: track 0.00 -> 61.7 mm, vias 0 -> 2
- net MEASURED_FUSE4: track 0.00 -> 59.5 mm, vias 0 -> 2
- net /MainBoard/SERVO0: track 98.7 -> 39.4 mm, vias 2 -> 1
- net +BATT: track 64.8 -> 13.4 mm, vias 16 -> 6
- net /MainBoard/SERVO19: track 43.4 -> 0.00 mm, vias 1 -> 0
- net MEASURED_FUSE1: track 0.00 -> 41.7 mm, vias 0 -> 2
- net /MainBoard/SERVO18: track 41.2 -> 0.00 mm, vias 1 -> 0
- net /MainBoard/IO14: track 0.00 -> 39.6 mm, vias 0 -> 2
- net MEASURED_FUSE2: track 0.00 -> 39.6 mm, vias 0 -> 2
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- removed copper zone on F.Cu, net +3.3VA
- removed copper zone on In1.Cu, net +3V3
- removed copper zone on F.Cu, net /MainBoard/Servos/6V1
- removed copper zone on F.Cu, net /MainBoard/Servos/6V2
- removed copper zone on F.Cu, net /MainBoard/Servos/6V3
- removed copper zone on F.Cu, net /MainBoard/Servos/6V4
- removed copper zone on F.Cu, net /MainBoard/Servos/6V5
- removed copper zone on F.Cu, net /MainBoard/Sheet5DD4BDB8/PHASE
- removed copper zone on F.Cu, net /MainBoard/Sheet5DD4BDB8/SRN
- removed copper zone on F.Cu, net /MainBoard/Sheet5DD4BDB8/SRP
- removed copper zone on F.Cu, net Net-(C49-Pad1)
- removed copper zone on F.Cu, net VBUS
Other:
- net class Default: via_drill 0.35 -> 0.2
- rule via_min_drill: 0.3 -> 0.2
